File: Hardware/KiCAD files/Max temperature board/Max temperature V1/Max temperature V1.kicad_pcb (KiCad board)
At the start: 2 copper layers, 52.1 x 22.9 mm, 18 parts, among them J1 Conn_01x06, U13 MAX31865, X1 3.5mm, X2 3.5mm

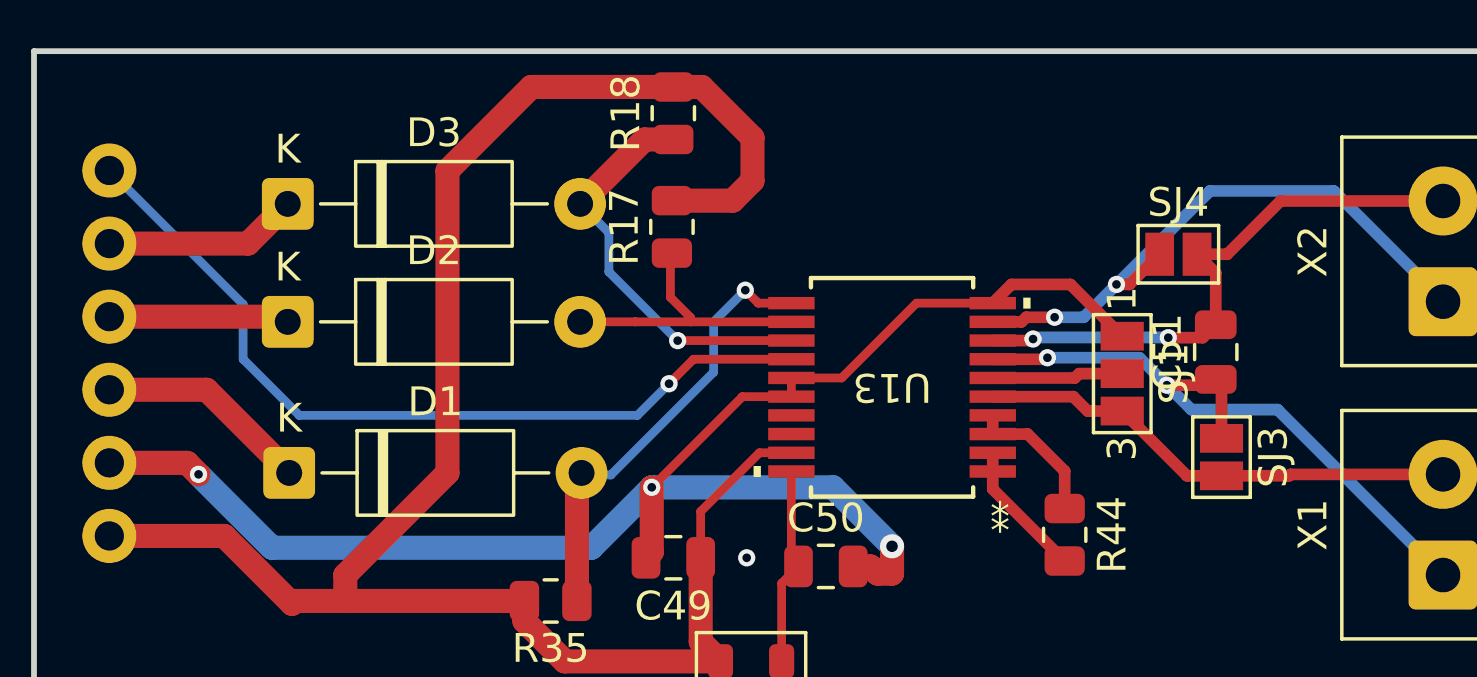
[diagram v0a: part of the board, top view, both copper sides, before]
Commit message: Compatability mods
basic modifications to work toward compatability between boards physically on the hotend
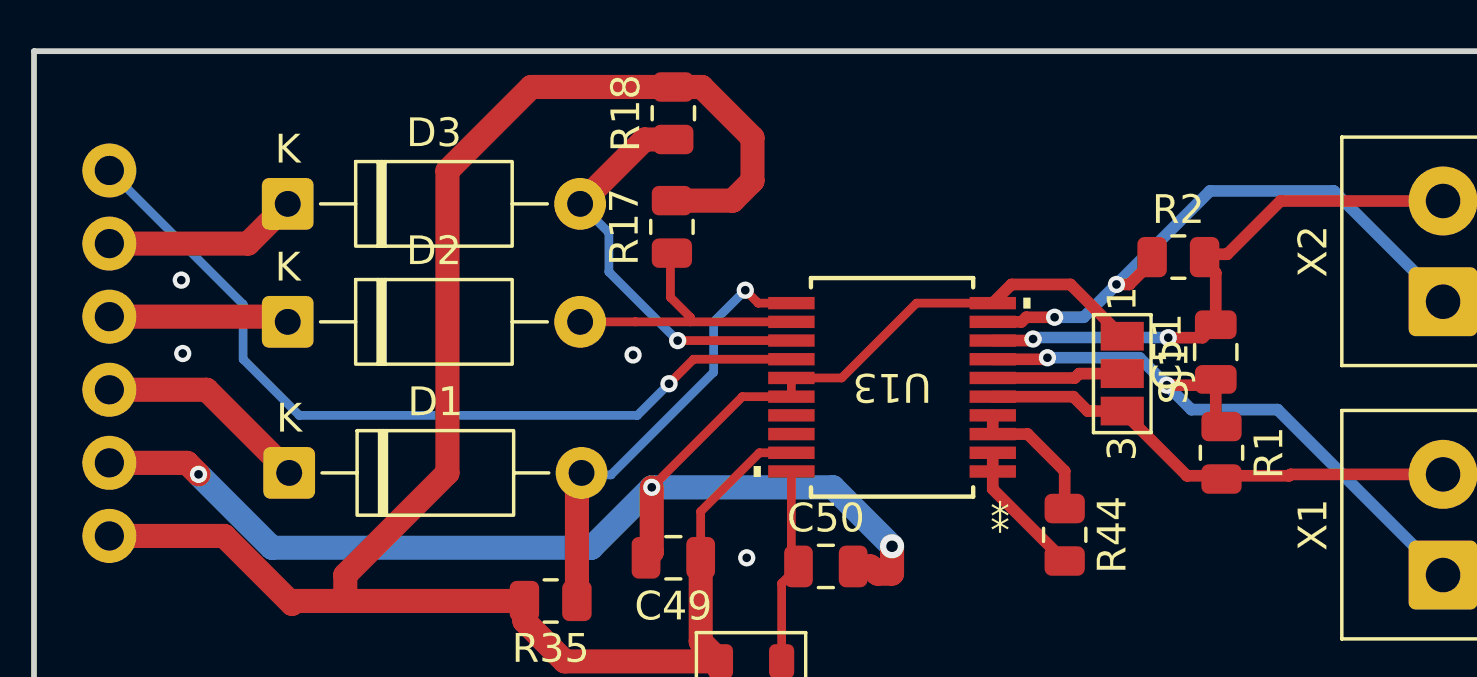
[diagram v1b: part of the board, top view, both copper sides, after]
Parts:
- removed SJ3, SJ4: SOLDERJUMPER, Jumper:SolderJumper-2_P1.3mm_Open_Pad1.0x1.5mm
- added R1: 0ohm, Resistor_SMD:R_0805_2012Metric, F.Cu at (121.3, 108.2)
- added R2: 0ohm, Resistor_SMD:R_0805_2012Metric, F.Cu at (119.8, 101.5)
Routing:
- net GND: vias 4 -> 7
